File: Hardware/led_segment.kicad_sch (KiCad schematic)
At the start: 28 parts

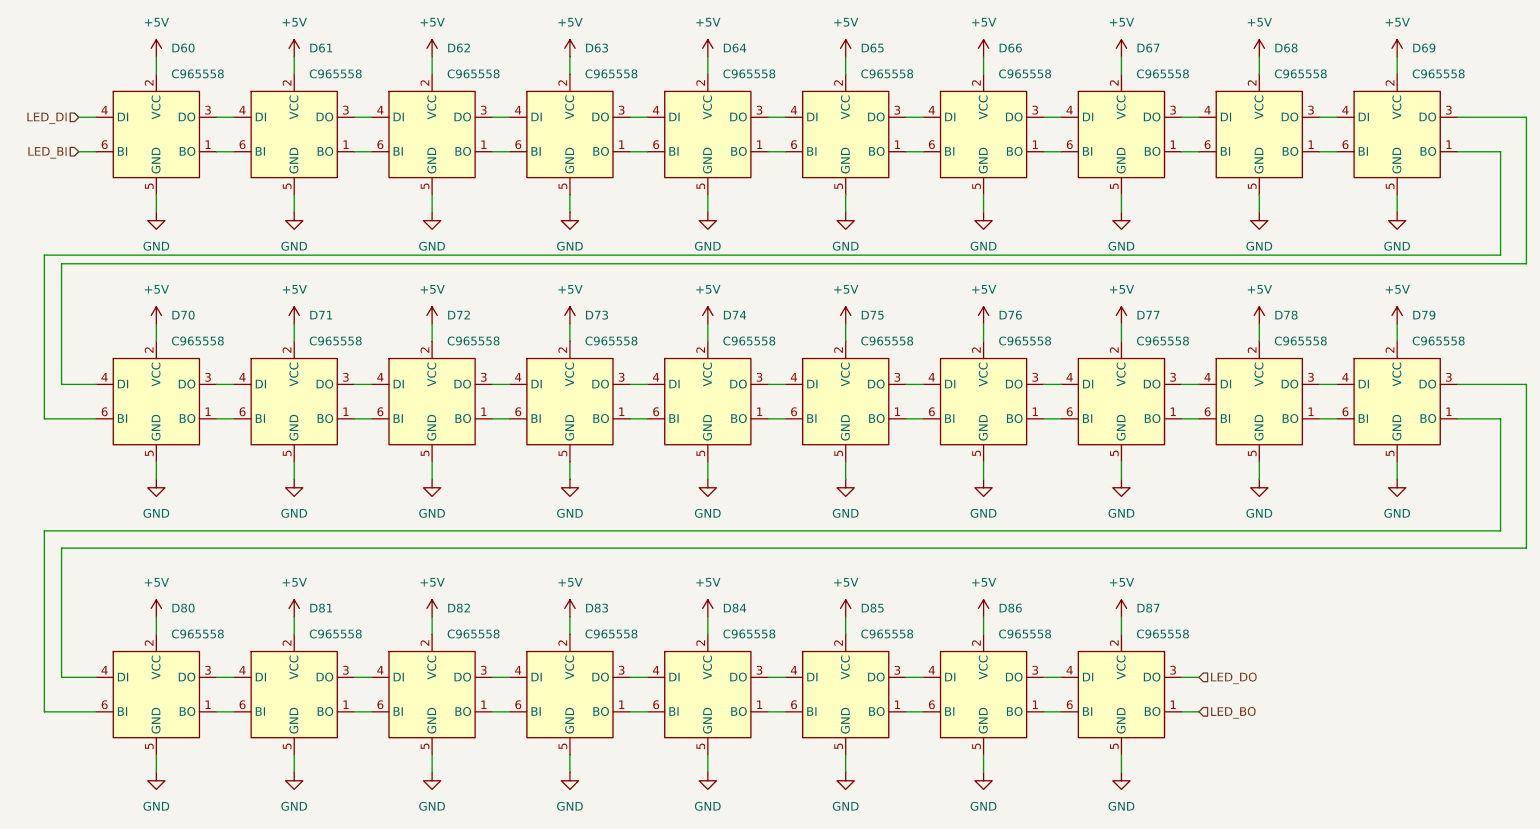
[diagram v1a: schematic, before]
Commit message: added LCSC number and datasheets
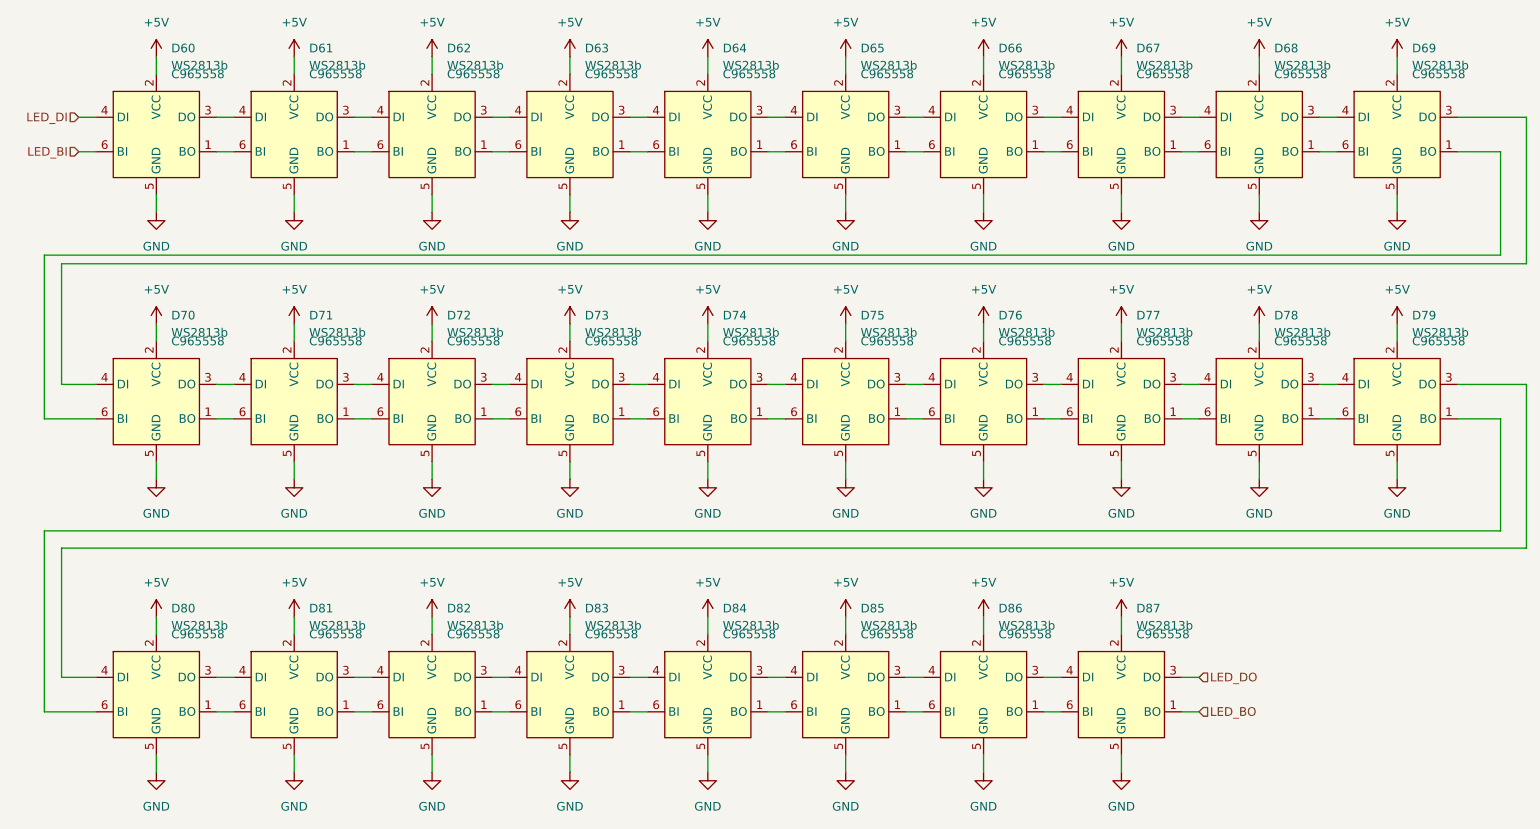
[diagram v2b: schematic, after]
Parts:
- D60, D61, D62, D63, D64, D65, D66, D67, D68, D69, D70, D71, D72, D73, D74, D75, D76, D77, D78, D79, D80, D81, D82, D83, D84, D85, D86, D87: value ~ -> WS2813b
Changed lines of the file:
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@@
 			)
 		)
-		(property "Value" "~"
+		(property "Value" "WS2813b"
 			(at 178.7241 173.99 0)
 			(effects
@@
 			)
 		)
-		(property "Value" "~"
+		(property "Value" "WS2813b"
 			(at 178.7241 91.44 0)
 			(effects
@@
 			)
 		)
-		(property "Value" "~"
+		(property "Value" "WS2813b"
 			(at 97.4441 130.81 0)
 			(effects
@@
 			)
 		)
-		(property "Value" "~"
+		(property "Value" "WS2813b"
 			(at 260.0041 91.44 0)
 			(effects
@@
 			)
 		)
-		(property "Value" "~"
+		(property "Value" "WS2813b"
 			(at 280.3241 130.81 0)
 			(effects
@@
 			)
 		)
-		(property "Value" "~"
+		(property "Value" "WS2813b"
 			(at 158.4041 173.99 0)
 			(effects
@@
 			)
 		)
-		(property "Value" "~"
+		(property "Value" "WS2813b"
 			(at 239.6841 130.81 0)
 			(effects
@@
 			)
 		)
-		(property "Value" "~"
+		(property "Value" "WS2813b"
 			(at 117.7641 173.99 0)
 			(effects
@@
 			)
 		)
-		(property "Value" "~"
+		(property "Value" "WS2813b"
 			(at 219.3641 130.81 0)
 			(effects
@@
 			)
 		)
-		(property "Value" "~"
+		(property "Value" "WS2813b"
 			(at 117.7641 91.44 0)
 			(effects
@@
 			)
 		)
-		(property "Value" "~"
+		(property "Value" "WS2813b"
 			(at 158.4041 130.81 0)
 			(effects
@@
 			)
 		)
-		(property "Value" "~"
+		(property "Value" "WS2813b"
 			(at 219.3641 91.44 0)
 			(effects
@@
 			)
 		)
-		(property "Value" "~"
+		(property "Value" "WS2813b"
 			(at 97.4441 91.44 0)
 			(effects
@@
 			)
 		)
-		(property "Value" "~"
+		(property "Value" "WS2813b"
 			(at 199.0441 130.81 0)
 			(effects
@@
 			)
 		)
-		(property "Value" "~"
+		(property "Value" "WS2813b"
 			(at 138.0841 91.44 0)
 			(effects
@@
 			)
 		)
-		(property "Value" "~"
+		(property "Value" "WS2813b"
 			(at 97.4441 173.99 0)
 			(effects
@@
 			)
 		)
-		(property "Value" "~"
+		(property "Value" "WS2813b"
 			(at 239.6841 91.44 0)
 			(effects
@@
 			)
 		)
-		(property "Value" "~"
+		(property "Value" "WS2813b"
 			(at 117.7641 130.81 0)
 			(effects
@@
 			)
 		)
-		(property "Value" "~"
+		(property "Value" "WS2813b"
 			(at 178.7241 130.81 0)
 			(effects
@@
 			)
 		)
-		(property "Value" "~"
+		(property "Value" "WS2813b"
 			(at 138.0841 130.81 0)
 			(effects
@@
 			)
 		)
-		(property "Value" "~"
+		(property "Value" "WS2813b"
 			(at 260.0041 130.81 0)
 			(effects
@@
 			)
 		)
-		(property "Value" "~"
+		(property "Value" "WS2813b"
 			(at 199.0441 173.99 0)
 			(effects
@@
 			)
 		)
-		(property "Value" "~"
+		(property "Value" "WS2813b"
 			(at 138.0841 173.99 0)
 			(effects
@@
 			)
 		)
-		(property "Value" "~"
+		(property "Value" "WS2813b"
 			(at 239.6841 173.99 0)
 			(effects
@@
 			)
 		)
-		(property "Value" "~"
+		(property "Value" "WS2813b"
 			(at 219.3641 173.99 0)
 			(effects
@@
 			)
 		)
-		(property "Value" "~"
+		(property "Value" "WS2813b"
 			(at 199.0441 91.44 0)
 			(effects
@@
 			)
 		)
-		(property "Value" "~"
+		(property "Value" "WS2813b"
 			(at 280.3241 91.44 0)
 			(effects
@@
 			)
 		)
-		(property "Value" "~"
+		(property "Value" "WS2813b"
 			(at 158.4041 91.44 0)
 			(effects

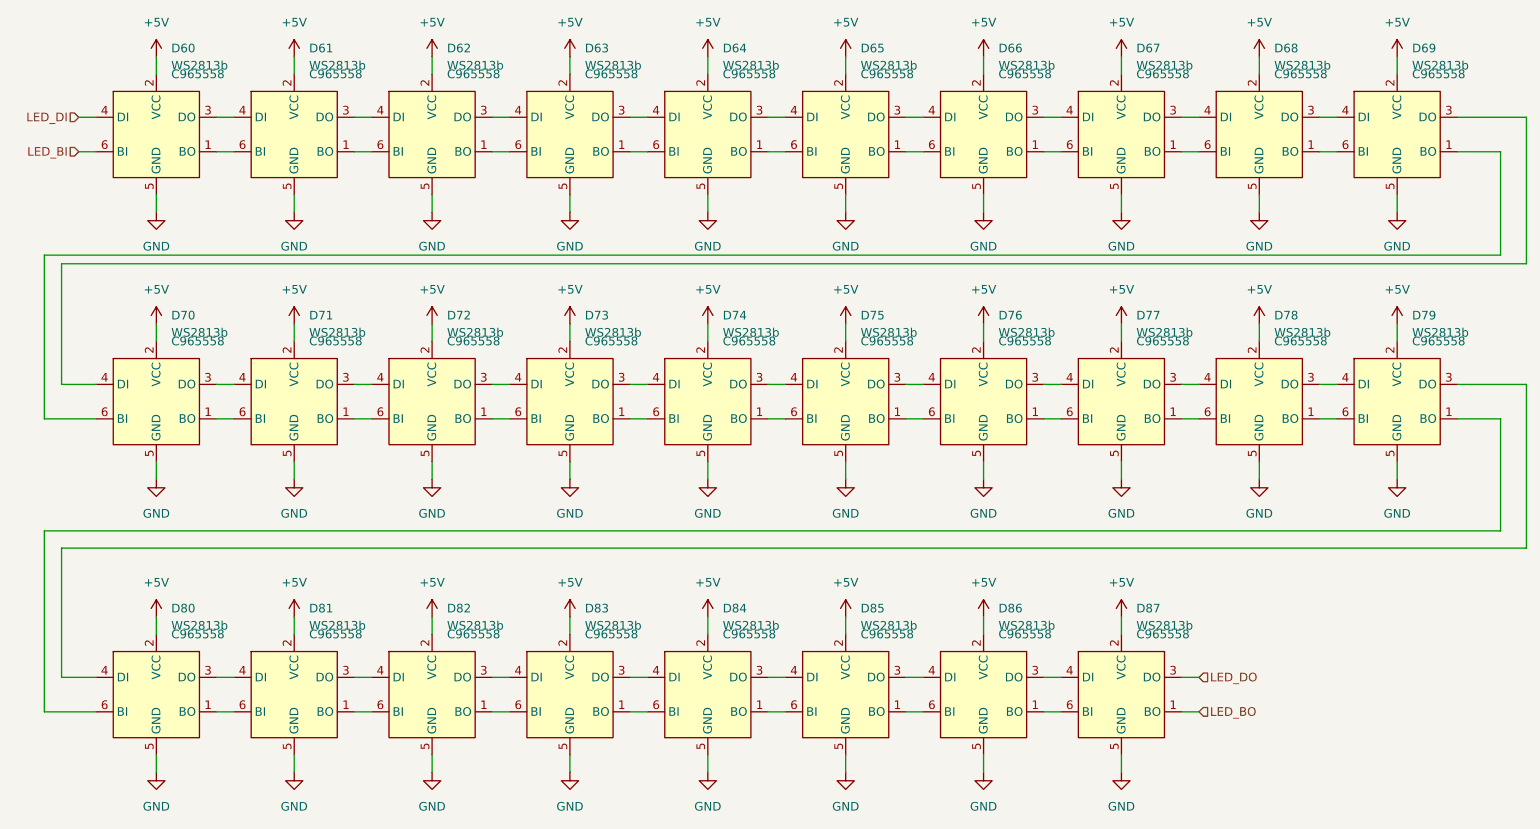
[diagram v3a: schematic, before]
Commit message: finalized layout, everything on top + LCSC numbers
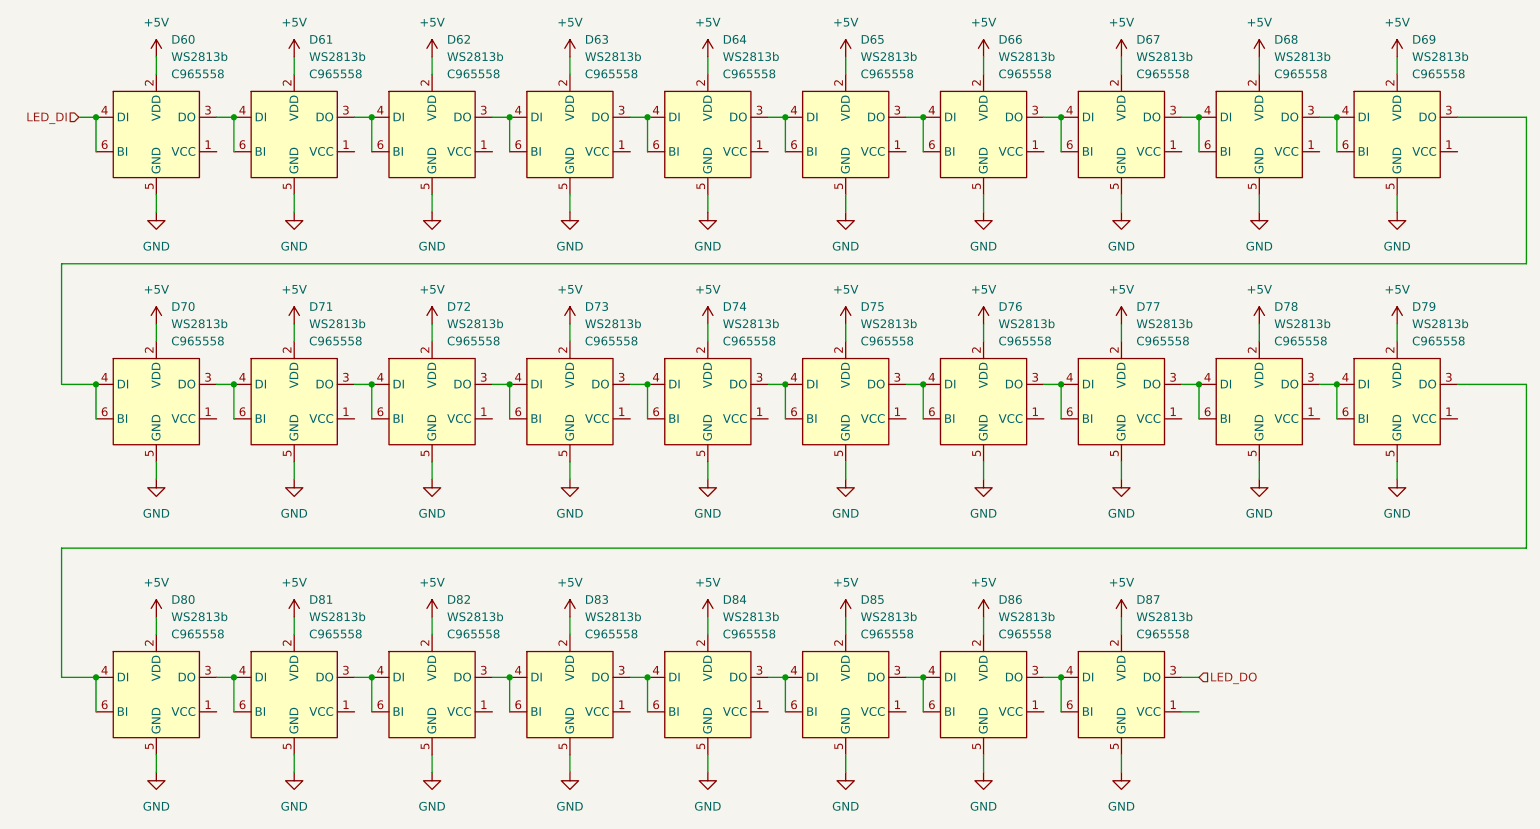
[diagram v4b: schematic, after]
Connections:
- net LED_BI is gone; now on net LED_DI: D60.6 (BI)
- net at D84.1 (VCC): no longer D85.6 (BI)
- net at D84.3 (DO), D85.4 (DI): now also D85.6 (BI)
- net at D83.3 (DO), D84.4 (DI): now also D84.6 (BI)
- net at D83.1 (VCC): no longer D84.6 (BI)
- net at D64.1 (VCC): no longer D65.6 (BI)
- net at D64.3 (DO), D65.4 (DI): now also D65.6 (BI)
- net at D63.3 (DO), D64.4 (DI): now also D64.6 (BI)
- net at D63.1 (VCC): no longer D64.6 (BI)
- net at D70.1 (VCC): no longer D71.6 (BI)
- net at D70.3 (DO), D71.4 (DI): now also D71.6 (BI)
- net at D69.3 (DO), D70.4 (DI): now also D70.6 (BI)
- net at D69.1 (VCC): no longer D70.6 (BI)
- net at D68.1 (VCC): no longer D69.6 (BI)
- net at D68.3 (DO), D69.4 (DI): now also D69.6 (BI)
- net at D67.3 (DO), D68.4 (DI): now also D68.6 (BI)
- net at D67.1 (VCC): no longer D68.6 (BI)
- net at D79.1 (VCC): no longer D80.6 (BI)
- net at D79.3 (DO), D80.4 (DI): now also D80.6 (BI)
- net at D78.3 (DO), D79.4 (DI): now also D79.6 (BI)
- net at D78.1 (VCC): no longer D79.6 (BI)
- net at D82.3 (DO), D83.4 (DI): now also D83.6 (BI)
- net at D82.1 (VCC): no longer D83.6 (BI)
- net at D77.1 (VCC): no longer D78.6 (BI)
- net at D77.3 (DO), D78.4 (DI): now also D78.6 (BI)
- net at D76.3 (DO), D77.4 (DI): now also D77.6 (BI)
- net at D76.1 (VCC): no longer D77.6 (BI)
- net at D81.1 (VCC): no longer D82.6 (BI)
- net at D81.3 (DO), D82.4 (DI): now also D82.6 (BI)
- net at D80.3 (DO), D81.4 (DI): now also D81.6 (BI)
- net at D80.1 (VCC): no longer D81.6 (BI)
- net at D75.3 (DO), D76.4 (DI): now also D76.6 (BI)
- net at D75.1 (VCC): no longer D76.6 (BI)
- net at D61.1 (VCC): no longer D62.6 (BI)
- net at D61.3 (DO), D62.4 (DI): now also D62.6 (BI)
- net at D60.3 (DO), D61.4 (DI): now also D61.6 (BI)
- net at D60.1 (VCC): no longer D61.6 (BI)
- net at D73.1 (VCC): no longer D74.6 (BI)
- net at D73.3 (DO), D74.4 (DI): now also D74.6 (BI)
- net at D72.3 (DO), D73.4 (DI): now also D73.6 (BI)
- net at D72.1 (VCC): no longer D73.6 (BI)
- net at D66.1 (VCC): no longer D67.6 (BI)
- net at D66.3 (DO), D67.4 (DI): now also D67.6 (BI)
- net at D65.3 (DO), D66.4 (DI): now also D66.6 (BI)
- net at D65.1 (VCC): no longer D66.6 (BI)
- net at D74.3 (DO), D75.4 (DI): now also D75.6 (BI)
- net at D74.1 (VCC): no longer D75.6 (BI)
- net at D62.1 (VCC): no longer D63.6 (BI)
- net at D62.3 (DO), D63.4 (DI): now also D63.6 (BI)
- net at D71.1 (VCC): no longer D72.6 (BI)
- net at D71.3 (DO), D72.4 (DI): now also D72.6 (BI)
- net at D85.1 (VCC): no longer D86.6 (BI)
- net at D85.3 (DO), D86.4 (DI): now also D86.6 (BI)
- net at D86.3 (DO), D87.4 (DI): now also D87.6 (BI)
- net at D86.1 (VCC): no longer D87.6 (BI)
- net LED_BO: no longer names the net of D87.1 (VCC)

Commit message: finalized layout, via stitching
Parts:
- D60, D61, D62, D63, D64, D65, D66, D67, D68, D69, D70, D71, D72, D73, D74, D75, D76, D77, D78, D79, D80, D81, D82, D83, D84, D85, D86, D87: LCSC C965558 -> C114592
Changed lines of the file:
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@@
 			)
 		)
-		(property "LCSC" "C965558"
+		(property "LCSC" "C114592"
 			(at 178.7241 175.26 0)
 			(effects
@@
 			)
 		)
-		(property "LCSC" "C965558"
+		(property "LCSC" "C114592"
 			(at 178.7241 92.71 0)
 			(effects
@@
 			)
 		)
-		(property "LCSC" "C965558"
+		(property "LCSC" "C114592"
 			(at 97.4441 132.08 0)
 			(effects
@@
 			)
 		)
-		(property "LCSC" "C965558"
+		(property "LCSC" "C114592"
 			(at 260.0041 92.71 0)
 			(effects
@@
 			)
 		)
-		(property "LCSC" "C965558"
+		(property "LCSC" "C114592"
 			(at 280.3241 132.08 0)
 			(effects
@@
 			)
 		)
-		(property "LCSC" "C965558"
+		(property "LCSC" "C114592"
 			(at 158.4041 175.26 0)
 			(effects
@@
 			)
 		)
-		(property "LCSC" "C965558"
+		(property "LCSC" "C114592"
 			(at 239.6841 132.08 0)
 			(effects
@@
 			)
 		)
-		(property "LCSC" "C965558"
+		(property "LCSC" "C114592"
 			(at 117.7641 175.26 0)
 			(effects
@@
 			)
 		)
-		(property "LCSC" "C965558"
+		(property "LCSC" "C114592"
 			(at 219.3641 132.08 0)
 			(effects
@@
 			)
 		)
-		(property "LCSC" "C965558"
+		(property "LCSC" "C114592"
 			(at 117.7641 92.71 0)
 			(effects
@@
 			)
 		)
-		(property "LCSC" "C965558"
+		(property "LCSC" "C114592"
 			(at 158.4041 132.08 0)
 			(effects
@@
 			)
 		)
-		(property "LCSC" "C965558"
+		(property "LCSC" "C114592"
 			(at 219.3641 92.71 0)
 			(effects
@@
 			)
 		)
-		(property "LCSC" "C965558"
+		(property "LCSC" "C114592"
 			(at 97.4441 92.71 0)
 			(effects
@@
 			)
 		)
-		(property "LCSC" "C965558"
+		(property "LCSC" "C114592"
 			(at 199.0441 132.08 0)
 			(effects
@@
 			)
 		)
-		(property "LCSC" "C965558"
+		(property "LCSC" "C114592"
 			(at 138.0841 92.71 0)
 			(effects
@@
 			)
 		)
-		(property "LCSC" "C965558"
+		(property "LCSC" "C114592"
 			(at 97.4441 175.26 0)
 			(effects
@@
 			)
 		)
-		(property "LCSC" "C965558"
+		(property "LCSC" "C114592"
 			(at 239.6841 92.71 0)
 			(effects
@@
 			)
 		)
-		(property "LCSC" "C965558"
+		(property "LCSC" "C114592"
 			(at 117.7641 132.08 0)
 			(effects
@@
 			)
 		)
-		(property "LCSC" "C965558"
+		(property "LCSC" "C114592"
 			(at 178.7241 132.08 0)
 			(effects
@@
 			)
 		)
-		(property "LCSC" "C965558"
+		(property "LCSC" "C114592"
 			(at 138.0841 132.08 0)
 			(effects
@@
 			)
 		)
-		(property "LCSC" "C965558"
+		(property "LCSC" "C114592"
 			(at 260.0041 132.08 0)
 			(effects
@@
 			)
 		)
-		(property "LCSC" "C965558"
+		(property "LCSC" "C114592"
 			(at 199.0441 175.26 0)
 			(effects
@@
 			)
 		)
-		(property "LCSC" "C965558"
+		(property "LCSC" "C114592"
 			(at 138.0841 175.26 0)
 			(effects
@@
 			)
 		)
-		(property "LCSC" "C965558"
+		(property "LCSC" "C114592"
 			(at 239.6841 175.26 0)
 			(effects
@@
 			)
 		)
-		(property "LCSC" "C965558"
+		(property "LCSC" "C114592"
 			(at 219.3641 175.26 0)
 			(effects
@@
 			)
 		)
-		(property "LCSC" "C965558"
+		(property "LCSC" "C114592"
 			(at 199.0441 92.71 0)
 			(effects
@@
 			)
 		)
-		(property "LCSC" "C965558"
+		(property "LCSC" "C114592"
 			(at 280.3241 92.71 0)
 			(effects
@@
 			)
 		)
-		(property "LCSC" "C965558"
+		(property "LCSC" "C114592"
 			(at 158.4041 92.71 0)
 			(effects

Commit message: updated lcsc numbers
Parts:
- D60, D61, D62, D63, D64, D65, D66, D67, D68, D69, D70, D71, D72, D73, D74, D75, D76, D77, D78, D79, D80, D81, D82, D83, D84, D85, D86, D87: lcsc_new (none) -> C114592
